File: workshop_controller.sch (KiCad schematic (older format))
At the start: 61 parts, among them J1 Conn_02x10_Odd_Even, J2 Conn_02x10_Odd_Even, J3 AudioJack3, J4 Micro_SD_Card, J5 Conn_02x25_Odd_Even, J6 Conn_01x05_Female, J7 LOGO_TOUCH, M1 Microphone4, SW1 SW_Push, SW2 SW_Push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

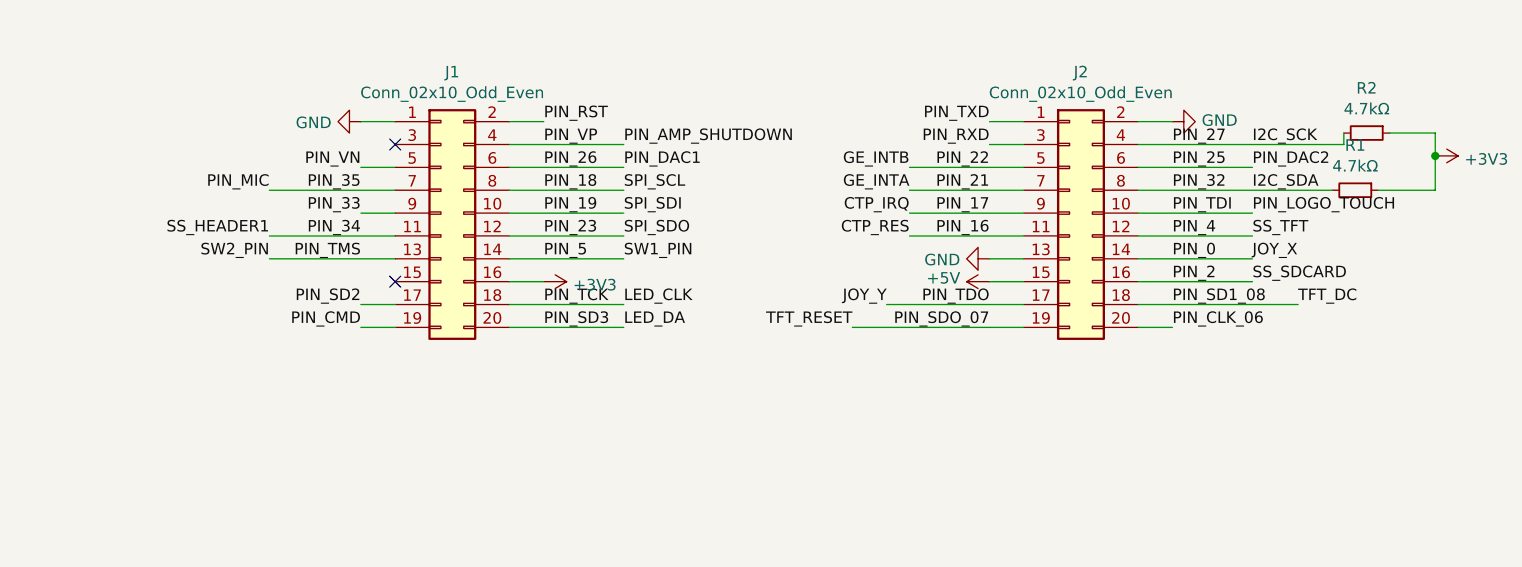
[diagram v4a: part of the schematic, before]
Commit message: Do design rules check
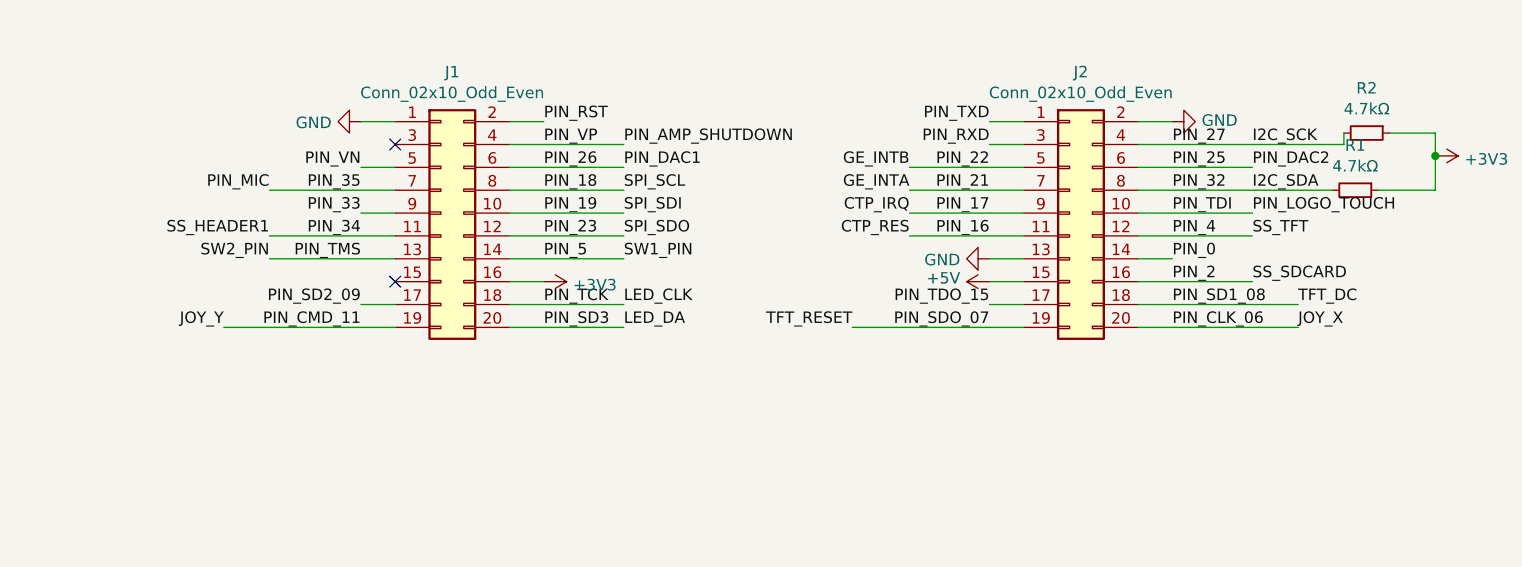
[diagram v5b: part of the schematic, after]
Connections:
- net labels added: PIN_CMD_11, PIN_SD2_09, PIN_TDO_15
- net labels removed: PIN_CMD, PIN_SD2, PIN_TDO
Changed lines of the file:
@@
 NoConn ~ 5900 6350
 Text Label 5750 6450 2    50   ~ 0
-PIN_SD2
+PIN_SD2_09
 Text Label 5750 6550 2    50   ~ 0
-PIN_CMD
+PIN_CMD_11
 Text Label 6550 6450 0    50   ~ 0
 PIN_TCK
@@
 $EndComp
 Text Label 8500 6450 2    50   ~ 0
-PIN_TDO
+PIN_TDO_15
 Text Label 8500 6550 2    50   ~ 0
 PIN_SDO_07
@@
 	8650 5750 8500 5750
 Wire Wire Line
-	9300 6550 9150 6550
-Wire Wire Line
 	5900 6450 5750 6450
-Wire Wire Line
-	5750 6550 5900 6550
 $Comp
 L power:+5V #PWR0104
@@
 Wire Wire Line
 	5750 6050 5900 6050
-Wire Wire Line
-	9150 6250 9650 6250
-Text Label 9650 6250 0    50   ~ 0
+Text Label 9850 6550 0    50   ~ 0
 JOY_X
-Text Label 8050 6450 2    50   ~ 0
+Text Label 5150 6550 2    50   ~ 0
 JOY_Y
-Wire Wire Line
-	8050 6450 8650 6450
 $Comp
 L Connector:Conn_01x01_Male J7
@@
 $EndComp
 $Comp
-L power:GND #PWR?
+L power:GND #PWR0175
 U 1 1 5CE73727
 P 14050 4100
-F 0 "#PWR?" H 14050 3850 50  0001 C CNN
+F 0 "#PWR0175" H 14050 3850 50  0001 C CNN
 F 1 "GND" V 14055 3972 50  0000 R CNN
 F 2 "" H 14050 4100 50  0001 C CNN
@@
 $EndComp
 $Comp
-L power:GND #PWR?
+L power:GND #PWR0189
 U 1 1 5CE73845
 P 15050 4100
-F 0 "#PWR?" H 15050 3850 50  0001 C CNN
+F 0 "#PWR0189" H 15050 3850 50  0001 C CNN
 F 1 "GND" V 15055 3972 50  0000 R CNN
 F 2 "" H 15050 4100 50  0001 C CNN
@@
 Wire Wire Line
 	8500 5650 8650 5650
+Wire Wire Line
+	9150 6550 9850 6550
+Wire Wire Line
+	9300 6250 9150 6250
+Wire Wire Line
+	5150 6550 5900 6550
+Wire Wire Line
+	8500 6450 8650 6450
 $EndSCHEMATC

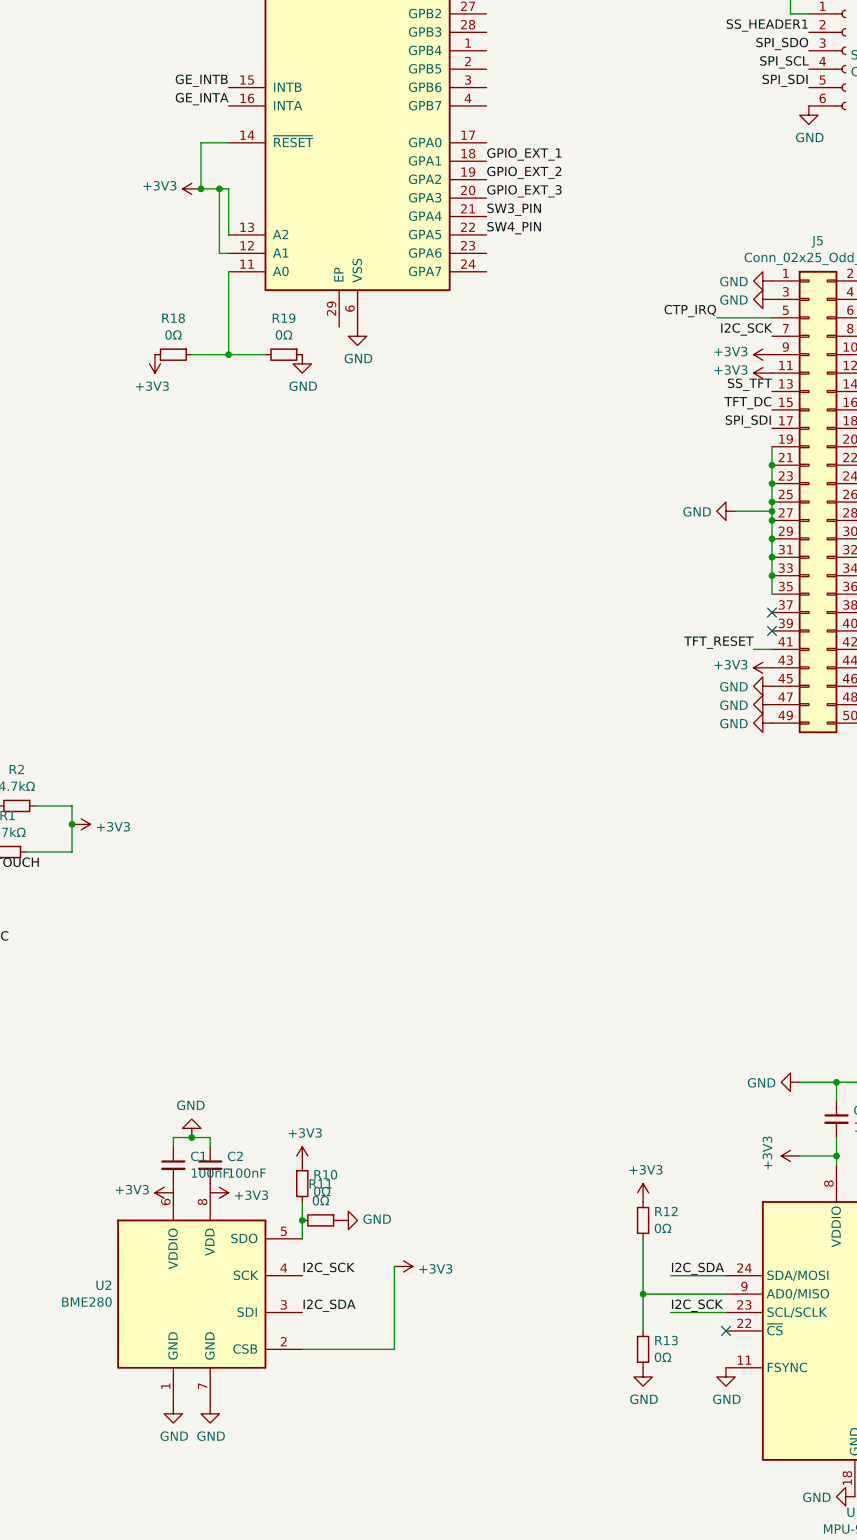
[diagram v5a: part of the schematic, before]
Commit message: Resolve I2C addresses
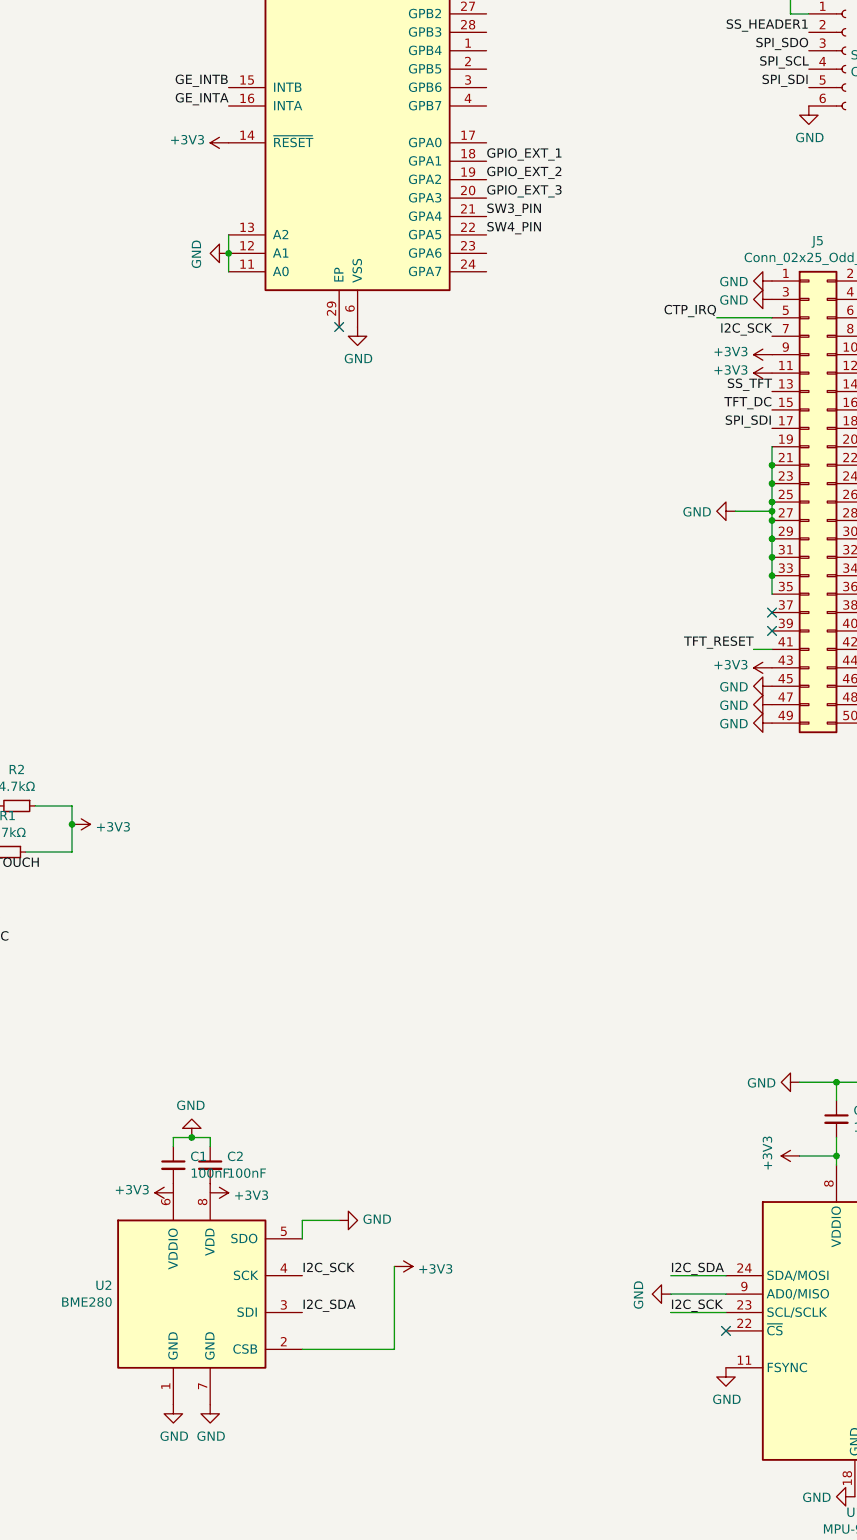
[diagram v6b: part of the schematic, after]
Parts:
- removed R10, R11, R12, R13, R18, R19: 0Ω, Resistor_SMD:R_0603_1608Metric_Pad1.05x0.95mm_HandSolder, symbol Device:R_Small
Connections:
- wire segments 168 -> 158
- no-connect marks 12 -> 13
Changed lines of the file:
@@
 	14450 1400 14350 1400
-$Comp
-L power:+3V3 #PWR0111
-U 1 1 5CA917C5
-P 11700 7650
-F 0 "#PWR0111" H 11700 7500 50  0001 C CNN
-F 1 "+3V3" H 11715 7823 50  0000 C CNN
-F 2 "" H 11700 7650 50  0001 C CNN
-F 3 "" H 11700 7650 50  0001 C CNN
-	1    11700 7650
-	1    0    0    -1
-$EndComp
 $Comp
 L power:GND #PWR0112
 U 1 1 5CAAD4CB
-P 13550 8750
-F 0 "#PWR0112" H 13550 8500 50  0001 C CNN
-F 1 "GND" H 13555 8577 50  0000 C CNN
-F 2 "" H 13550 8750 50  0001 C CNN
-F 3 "" H 13550 8750 50  0001 C CNN
-	1    13550 8750
-	1    0    0    -1
+P 13700 8350
+F 0 "#PWR0112" H 13700 8100 50  0001 C CNN
+F 1 "GND" H 13705 8177 50  0000 C CNN
+F 2 "" H 13700 8350 50  0001 C CNN
+F 3 "" H 13700 8350 50  0001 C CNN
+	1    13700 8350
+	0    1    1    0
 $EndComp
 Wire Wire Line
@@
 NoConn ~ 14000 8550
 $Comp
-L Device:R_Small R12
-U 1 1 5CB08528
-P 13550 7950
-F 0 "R12" H 13609 7996 50  0000 L CNN
-F 1 "0Ω" H 13609 7905 50  0000 L CNN
-F 2 "Resistor_SMD:R_0603_1608Metric_Pad1.05x0.95mm_HandSolder" H 13550 7950 50  0001 C CNN
-F 3 "~" H 13550 7950 50  0001 C CNN
-	1    13550 7950
-	1    0    0    -1
-$EndComp
-$Comp
-L Device:R_Small R13
-U 1 1 5CB085A3
-P 13550 8650
-F 0 "R13" H 13609 8696 50  0000 L CNN
-F 1 "0Ω" H 13609 8605 50  0000 L CNN
-F 2 "Resistor_SMD:R_0603_1608Metric_Pad1.05x0.95mm_HandSolder" H 13550 8650 50  0001 C CNN
-F 3 "~" H 13550 8650 50  0001 C CNN
-	1    13550 8650
-	1    0    0    -1
-$EndComp
-Wire Wire Line
-	13550 8350 13550 8050
-$Comp
-L power:+3V3 #PWR0117
-U 1 1 5CB0C3C5
-P 13550 7850
-F 0 "#PWR0117" H 13550 7700 50  0001 C CNN
-F 1 "+3V3" H 13565 8023 50  0000 C CNN
-F 2 "" H 13550 7850 50  0001 C CNN
-F 3 "" H 13550 7850 50  0001 C CNN
-	1    13550 7850
-	1    0    0    -1
-$EndComp
-Wire Wire Line
-	13550 8550 13550 8350
-Connection ~ 13550 8350
-$Comp
 L Device:C_Small C1
 U 1 1 5CB26720
@@
 $EndComp
 $Comp
-L Device:R_Small R10
-U 1 1 5CB6002C
-P 11700 7750
-F 0 "R10" H 11759 7796 50  0000 L CNN
-F 1 "0Ω" H 11759 7705 50  0000 L CNN
-F 2 "Resistor_SMD:R_0603_1608Metric_Pad1.05x0.95mm_HandSolder" H 11700 7750 50  0001 C CNN
-F 3 "~" H 11700 7750 50  0001 C CNN
-	1    11700 7750
-	1    0    0    -1
-$EndComp
-$Comp
 L Sensor:BME280 U2
 U 1 1 5CA64E9A
@@
 	1    11100 8350
 	1    0    0    -1
-$EndComp
-$Comp
-L Device:R_Small R11
-U 1 1 5CB80FEA
-P 11800 7950
-F 0 "R11" V 11604 7950 50  0000 C CNN
-F 1 "0Ω" V 11695 7950 50  0000 C CNN
-F 2 "Resistor_SMD:R_0603_1608Metric_Pad1.05x0.95mm_HandSolder" H 11800 7950 50  0001 C CNN
-F 3 "~" H 11800 7950 50  0001 C CNN
-	1    11800 7950
-	0    1    1    0
 $EndComp
 Wire Wire Line
@@
 Wire Wire Line
 	14000 8450 13700 8450
-Wire Wire Line
-	13550 8350 14000 8350
 $Comp
 L power:GND #PWR0124
@@
 Text Label 10100 10100 2    50   ~ 0
 I2C_SCK
-Connection ~ 11700 7950
 Wire Wire Line
 	11700 7950 11700 8050
-Wire Wire Line
-	11700 7850 11700 7950
 $Comp
 L workshop_controller-rescue:TPA6203A1-bytebarista U4
@@
 Text Label 4600 1500 0    50   ~ 0
 PIN_DAC2
-$Comp
-L power:GND #PWR0156
-U 1 1 5CBFD31D
-P 12000 3100
-F 0 "#PWR0156" H 12000 2850 50  0001 C CNN
-F 1 "GND" H 12005 2927 50  0000 C CNN
-F 2 "" H 12000 3100 50  0001 C CNN
-F 3 "" H 12000 3100 50  0001 C CNN
-	1    12000 3100
-	1    0    0    -1
-$EndComp
 $Comp
 L workshop_controller-rescue:APA102-GSG D2
@@
 L power:+3V3 #PWR0167
 U 1 1 5CC68DDB
-P 11150 2350
-F 0 "#PWR0167" H 11150 2200 50  0001 C CNN
-F 1 "+3V3" V 11165 2478 50  0000 L CNN
-F 2 "" H 11150 2350 50  0001 C CNN
-F 3 "" H 11150 2350 50  0001 C CNN
-	1    11150 2350
+P 11300 2100
+F 0 "#PWR0167" H 11300 1950 50  0001 C CNN
+F 1 "+3V3" V 11315 2228 50  0000 L CNN
+F 2 "" H 11300 2100 50  0001 C CNN
+F 3 "" H 11300 2100 50  0001 C CNN
+	1    11300 2100
 	0    -1   -1   0
-$EndComp
-Wire Wire Line
-	11300 2100 11150 2100
-Wire Wire Line
-	11150 2100 11150 2350
-Wire Wire Line
-	11300 2600 11300 2350
-Wire Wire Line
-	11300 2350 11250 2350
-Connection ~ 11150 2350
-Wire Wire Line
-	11300 2700 11250 2700
-Wire Wire Line
-	11250 2700 11250 2350
-Connection ~ 11250 2350
-Wire Wire Line
-	11250 2350 11150 2350
-Wire Wire Line
-	11300 2800 11300 3250
-Wire Wire Line
-	11300 3250 11100 3250
-$Comp
-L Device:R_Small R18
-U 1 1 5CC8ADDC
-P 11000 3250
-F 0 "R18" V 10804 3250 50  0000 C CNN
-F 1 "0Ω" V 10895 3250 50  0000 C CNN
-F 2 "Resistor_SMD:R_0603_1608Metric_Pad1.05x0.95mm_HandSolder" H 11000 3250 50  0001 C CNN
-F 3 "~" H 11000 3250 50  0001 C CNN
-	1    11000 3250
-	0    1    1    0
-$EndComp
-$Comp
-L Device:R_Small R19
-U 1 1 5CC8B193
-P 11600 3250
-F 0 "R19" V 11404 3250 50  0000 C CNN
-F 1 "0Ω" V 11495 3250 50  0000 C CNN
-F 2 "Resistor_SMD:R_0603_1608Metric_Pad1.05x0.95mm_HandSolder" H 11600 3250 50  0001 C CNN
-F 3 "~" H 11600 3250 50  0001 C CNN
-	1    11600 3250
-	0    1    1    0
-$EndComp
-Wire Wire Line
-	11300 3250 11500 3250
-Connection ~ 11300 3250
-$Comp
-L power:+3V3 #PWR0168
-U 1 1 5CC92387
-P 10900 3250
-F 0 "#PWR0168" H 10900 3100 50  0001 C CNN
-F 1 "+3V3" H 10915 3423 50  0000 C CNN
-F 2 "" H 10900 3250 50  0001 C CNN
-F 3 "" H 10900 3250 50  0001 C CNN
-	1    10900 3250
-	-1   0    0    1
 $EndComp
 $Comp
 L power:GND #PWR0169
 U 1 1 5CC92505
-P 11700 3250
-F 0 "#PWR0169" H 11700 3000 50  0001 C CNN
-F 1 "GND" H 11705 3077 50  0000 C CNN
-F 2 "" H 11700 3250 50  0001 C CNN
-F 3 "" H 11700 3250 50  0001 C CNN
-	1    11700 3250
-	1    0    0    -1
+P 11300 2700
+F 0 "#PWR0169" H 11300 2450 50  0001 C CNN
+F 1 "GND" H 11305 2527 50  0000 C CNN
+F 2 "" H 11300 2700 50  0001 C CNN
+F 3 "" H 11300 2700 50  0001 C CNN
+	1    11300 2700
+	0    1    1    0
 $EndComp
 Text Label 11300 1800 2    50   ~ 0
@@
 Wire Wire Line
 	8500 6450 8650 6450
+Wire Wire Line
+	11700 7950 11900 7950
+$Comp
+L power:GND #PWR0156
+U 1 1 5CBFD31D
+P 12000 3100
+F 0 "#PWR0156" H 12000 2850 50  0001 C CNN
+F 1 "GND" H 12005 2927 50  0000 C CNN
+F 2 "" H 12000 3100 50  0001 C CNN
+F 3 "" H 12000 3100 50  0001 C CNN
+	1    12000 3100
+	1    0    0    -1
+$EndComp
+Wire Wire Line
+	13700 8350 14000 8350
+NoConn ~ 11900 3100
+Wire Wire Line
+	11300 2600 11300 2700
+Connection ~ 11300 2700
+Wire Wire Line
+	11300 2700 11300 2800
 $EndSCHEMATC

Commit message: Change R3-R7 footprints to 0603
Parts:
- R3, R4, R5, R6, R7: footprint Resistor_SMD:R_1206_3216Metric_Pad1.42x1.75mm_HandSolder -> Resistor_SMD:R_0603_1608Metric_Pad1.05x0.95mm_HandSolder
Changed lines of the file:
@@
 F 0 "R3" V 7104 1550 50  0000 C CNN
 F 1 "50kΩ" V 7195 1550 50  0000 C CNN
-F 2 "Resistor_SMD:R_1206_3216Metric_Pad1.42x1.75mm_HandSolder" H 7300 1550 50  0001 C CNN
+F 2 "Resistor_SMD:R_0603_1608Metric_Pad1.05x0.95mm_HandSolder" H 7300 1550 50  0001 C CNN
 F 3 "~" H 7300 1550 50  0001 C CNN
 	1    7300 1550
@@
 F 0 "R4" V 7104 1650 50  0000 C CNN
 F 1 "50kΩ" V 7195 1650 50  0000 C CNN
-F 2 "Resistor_SMD:R_1206_3216Metric_Pad1.42x1.75mm_HandSolder" H 7300 1650 50  0001 C CNN
+F 2 "Resistor_SMD:R_0603_1608Metric_Pad1.05x0.95mm_HandSolder" H 7300 1650 50  0001 C CNN
 F 3 "~" H 7300 1650 50  0001 C CNN
 	1    7300 1650
@@
 F 0 "R5" V 7104 1750 50  0000 C CNN
 F 1 "50kΩ" V 7195 1750 50  0000 C CNN
-F 2 "Resistor_SMD:R_1206_3216Metric_Pad1.42x1.75mm_HandSolder" H 7300 1750 50  0001 C CNN
+F 2 "Resistor_SMD:R_0603_1608Metric_Pad1.05x0.95mm_HandSolder" H 7300 1750 50  0001 C CNN
 F 3 "~" H 7300 1750 50  0001 C CNN
 	1    7300 1750
@@
 F 0 "R6" V 7104 2150 50  0000 C CNN
 F 1 "50kΩ" V 7195 2150 50  0000 C CNN
-F 2 "Resistor_SMD:R_1206_3216Metric_Pad1.42x1.75mm_HandSolder" H 7300 2150 50  0001 C CNN
+F 2 "Resistor_SMD:R_0603_1608Metric_Pad1.05x0.95mm_HandSolder" H 7300 2150 50  0001 C CNN
 F 3 "~" H 7300 2150 50  0001 C CNN
 	1    7300 2150
@@
 F 0 "R7" V 7104 2250 50  0000 C CNN
 F 1 "50kΩ" V 7195 2250 50  0000 C CNN
-F 2 "Resistor_SMD:R_1206_3216Metric_Pad1.42x1.75mm_HandSolder" H 7300 2250 50  0001 C CNN
+F 2 "Resistor_SMD:R_0603_1608Metric_Pad1.05x0.95mm_HandSolder" H 7300 2250 50  0001 C CNN
 F 3 "~" H 7300 2250 50  0001 C CNN
 	1    7300 2250

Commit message: Add pin numbers to esp32
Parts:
- removed J3: AudioJack3, Connector_Audio:Jack_3.5mm_CUI_SJ1-3533NG_Horizontal, symbol Connector:AudioJack3
- added J3: AudioJack4, Connector_Audio:Jack_3.5mm_PJ320D_Horizontal, symbol Connector:AudioJack4
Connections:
- net labels added: PIN_TDI_12, PIN_TMS_14, PIN_VN_39, PIN_VP_36
- net labels removed: PIN_TDI, PIN_TMS, PIN_VN, PIN_VP
- wire segments 158 -> 162
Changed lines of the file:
@@
 PIN_34
 Text Label 5750 6250 2    50   ~ 0
-PIN_TMS
+PIN_TMS_14
 NoConn ~ 5900 6350
 Text Label 5750 6450 2    50   ~ 0
@@
 PIN_32
 Text Label 9300 6050 0    50   ~ 0
-PIN_TDI
+PIN_TDI_12
 Text Label 9300 6150 0    50   ~ 0
 PIN_4
@@
 PIN_RST
 Text Label 6550 5750 0    50   ~ 0
-PIN_VP
+PIN_VP_36
 Text Label 5750 5850 2    50   ~ 0
-PIN_VN
+PIN_VN_39
 Wire Wire Line
 	5750 5850 5900 5850
@@
 F 3 "" H 4850 8650 50  0001 C CNN
 	1    4850 8450
-	1    0    0    -1
-$EndComp
-$Comp
-L Connector:AudioJack3 J3
-U 1 1 5CA656CD
-P 4400 1400
-F 0 "J3" H 4380 1725 50  0000 C CNN
-F 1 "AudioJack3" H 4380 1634 50  0000 C CNN
-F 2 "Connector_Audio:Jack_3.5mm_CUI_SJ1-3533NG_Horizontal" H 4400 1400 50  0001 C CNN
-F 3 "~" H 4400 1400 50  0001 C CNN
-	1    4400 1400
 	1    0    0    -1
 $EndComp
@@
 Wire Wire Line
 	6400 6250 6900 6250
-Text Label 5350 6250 2    50   ~ 0
+Text Label 5200 6250 2    50   ~ 0
 SW2_PIN
-Wire Wire Line
-	5350 6250 5900 6250
 Text Label 6900 5850 0    50   ~ 0
 PIN_DAC1
@@
 Wire Wire Line
 	3150 1100 3350 1100
-$Comp
-L power:GND #PWR0155
-U 1 1 5CBF4395
-P 4600 1300
-F 0 "#PWR0155" H 4600 1050 50  0001 C CNN
-F 1 "GND" V 4605 1172 50  0000 R CNN
-F 2 "" H 4600 1300 50  0001 C CNN
-F 3 "" H 4600 1300 50  0001 C CNN
-	1    4600 1300
-	0    -1   -1   0
-$EndComp
-Text Label 4600 1400 0    50   ~ 0
-PIN_DAC1
-Text Label 4600 1500 0    50   ~ 0
-PIN_DAC2
 $Comp
 L workshop_controller-rescue:APA102-GSG D2
@@
 	1    0    0    -1
 $EndComp
-Text Label 9650 6050 0    50   ~ 0
+Text Label 9800 6050 0    50   ~ 0
 PIN_LOGO_TOUCH
 Text Label 4400 2400 0    50   ~ 0
 PIN_LOGO_TOUCH
-Wire Wire Line
-	9150 6050 9650 6050
 Text Label 6900 6550 0    50   ~ 0
 LED_DA
@@
 Text Label 1950 2150 2    50   ~ 0
 PIN_AMP_SHUTDOWN
-Text Label 6900 5750 0    50   ~ 0
+Text Label 7000 5750 0    50   ~ 0
 PIN_AMP_SHUTDOWN
-Wire Wire Line
-	6400 5750 6900 5750
 NoConn ~ 14750 3350
 NoConn ~ 14750 3550
@@
 Wire Wire Line
 	11300 2700 11300 2800
+$Comp
+L power:GND #PWR0111
+U 1 1 5CFE7CD2
+P 5150 1350
+F 0 "#PWR0111" H 5150 1100 50  0001 C CNN
+F 1 "GND" V 5155 1222 50  0000 R CNN
+F 2 "" H 5150 1350 50  0001 C CNN
+F 3 "" H 5150 1350 50  0001 C CNN
+	1    5150 1350
+	0    -1   -1   0
+$EndComp
+Text Label 5300 1550 0    50   ~ 0
+PIN_DAC1
+Text Label 5150 1650 0    50   ~ 0
+PIN_DAC2
+$Comp
+L Connector:AudioJack4 J3
+U 1 1 5CFE7CDA
+P 4950 1450
+F 0 "J3" H 4905 1775 50  0000 C CNN
+F 1 "AudioJack4" H 4905 1684 50  0000 C CNN
+F 2 "Connector_Audio:Jack_3.5mm_PJ320D_Horizontal" H 4950 1450 50  0001 C CNN
+F 3 "~" H 4950 1450 50  0001 C CNN
+	1    4950 1450
+	1    0    0    -1
+$EndComp
+Wire Wire Line
+	5150 1550 5200 1550
+Wire Wire Line
+	5150 1450 5200 1450
+Wire Wire Line
+	5200 1450 5200 1550
+Connection ~ 5200 1550
+Wire Wire Line
+	5200 1550 5300 1550
+Wire Wire Line
+	5200 6250 5900 6250
+Wire Wire Line
+	6400 5750 7000 5750
+Wire Wire Line
+	9150 6050 9800 6050
 $EndSCHEMATC
